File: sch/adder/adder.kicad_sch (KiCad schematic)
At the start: 40 parts

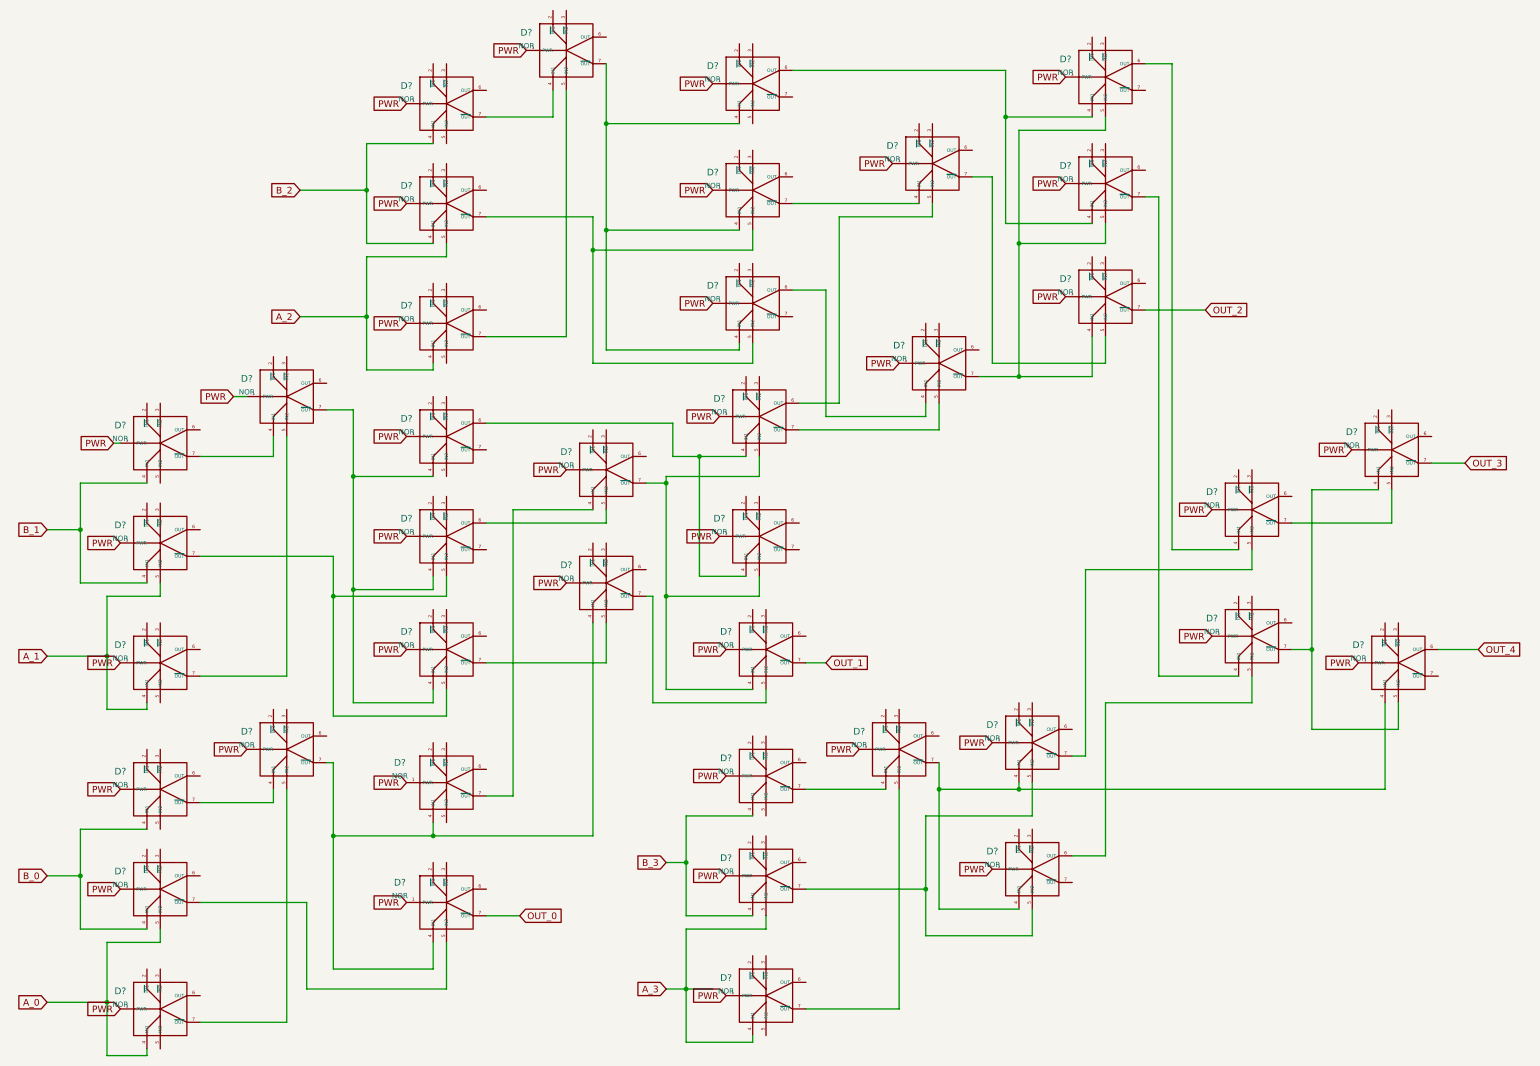
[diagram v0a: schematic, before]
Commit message: Manual import of 4bit adder to kicad
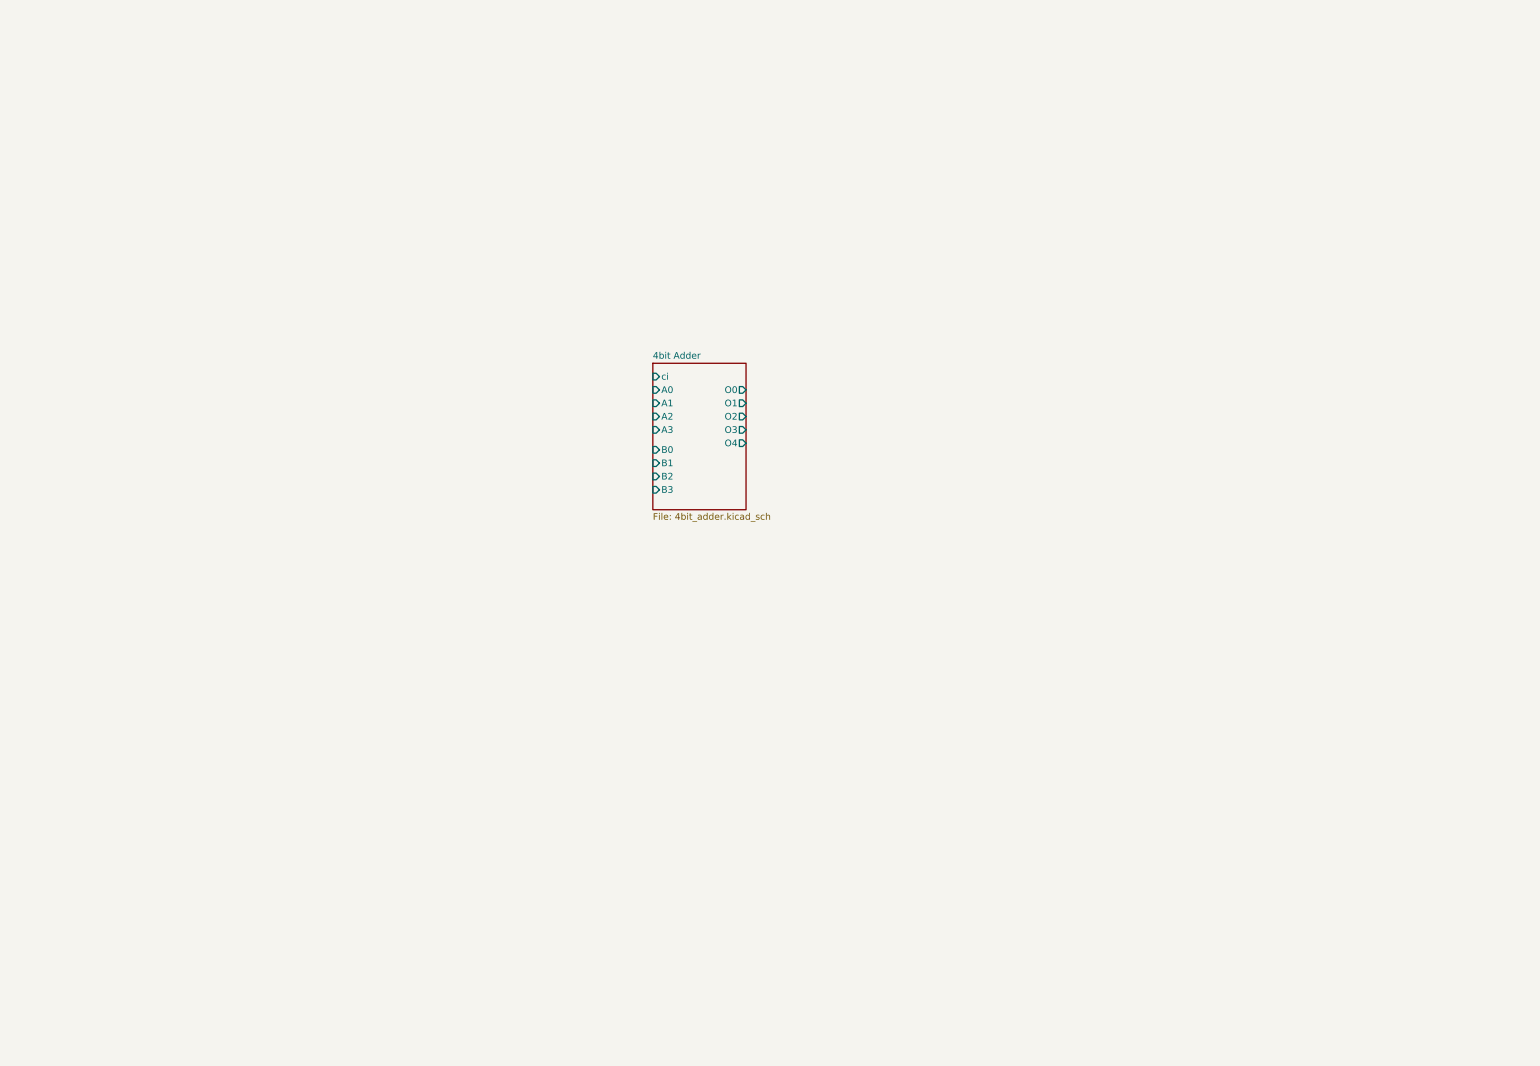
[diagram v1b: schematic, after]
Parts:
- removed D? (x40): NOR, symbol fluidic:NOR
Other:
- added sheet 4bit Adder (4bit_adder.kicad_sch)
